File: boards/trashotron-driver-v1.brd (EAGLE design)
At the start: 76.2 x 63.5 mm, 11 parts, among them IC1 2967-MP6500, IC2 2967-MP6500, IC3 2967-MP6500, J2 455-1750-1-ND, J4 455-1750-1-ND, J6 455-1750-1-ND

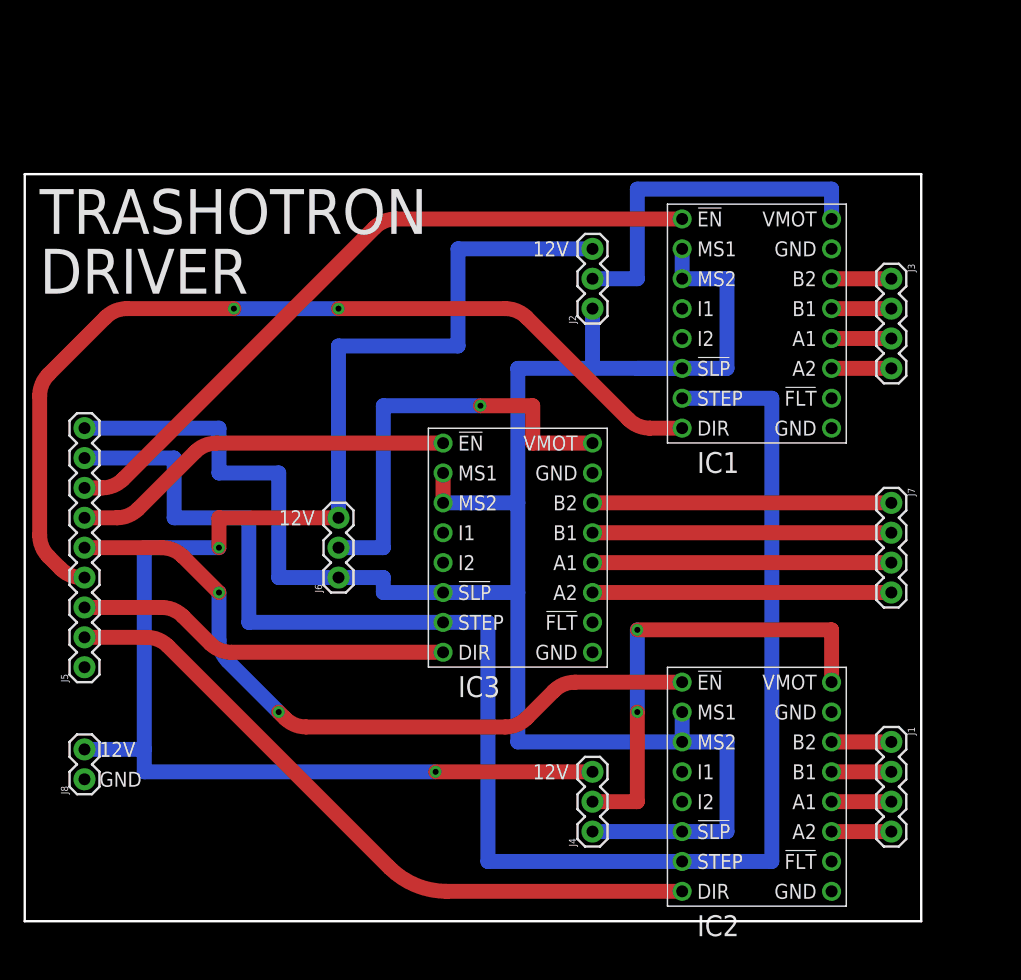
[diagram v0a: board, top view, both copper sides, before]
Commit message: board development and  a longer default glyph
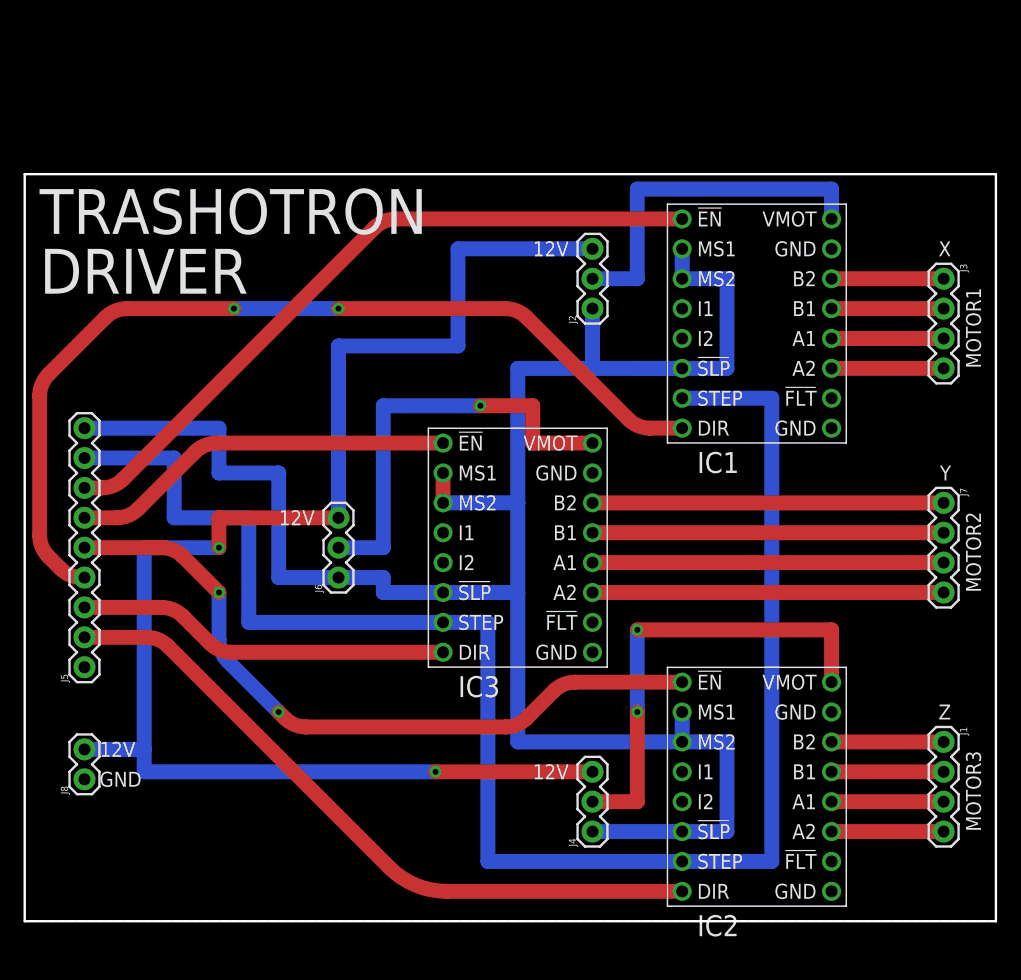
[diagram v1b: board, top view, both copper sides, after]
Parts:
- moved J1 4.45 mm to (78.1, 15.2)
- moved J3 4.45 mm to (78.1, 54.6)
- moved J7 4.45 mm to (78.1, 35.6)
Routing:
- net N$9: track 5.08 -> 9.53 mm
- net N$8: track 5.08 -> 9.53 mm
- net N$7: track 5.08 -> 9.53 mm
- net N$6: track 5.08 -> 9.53 mm
- net N$5: track 5.08 -> 9.53 mm
- net N$4: track 25.4 -> 29.8 mm
- net N$14: track 25.4 -> 29.8 mm
- net N$13: track 25.4 -> 29.8 mm
- net N$12: track 5.08 -> 9.53 mm
- net N$11: track 5.08 -> 9.53 mm
- net N$10: track 5.08 -> 9.53 mm
- net N$1: track 25.4 -> 29.8 mm
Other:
- board size 76.2 x 63.5 mm -> 82.5 x 63.5 mm
- board text added: "MOTOR1"
- board text added: "MOTOR2"
- board text added: "MOTOR3"
- board text added: "X"
- board text added: "Y"
- board text added: "Z"
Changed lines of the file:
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@@
 <board>
 <plain>
-<wire x1="76.2" y1="0" x2="76.2" y2="63.5" width="0.2032" layer="20"/>
-<wire x1="76.2" y1="63.5" x2="0" y2="63.5" width="0.2032" layer="20"/>
+<wire x1="82.55" y1="0" x2="82.55" y2="63.5" width="0.2032" layer="20"/>
+<wire x1="82.55" y1="63.5" x2="0" y2="63.5" width="0.2032" layer="20"/>
 <wire x1="0" y1="63.5" x2="0" y2="0" width="0.2032" layer="20"/>
-<wire x1="0" y1="0" x2="76.2" y2="0" width="0.2032" layer="20"/>
+<wire x1="0" y1="0" x2="82.55" y2="0" width="0.2032" layer="20"/>
 <wire x1="15.494" y1="0.508" x2="15.494" y2="29.21" width="0.0762" layer="51"/>
 <text x="-7.62" y="-5.08" size="2.286" layer="27">Arduino Wee v1.3</text>
@@
 <text x="43.18" y="12.065" size="1.27" layer="21">12V</text>
 <text x="21.59" y="33.655" size="1.27" layer="21">12V</text>
+<text x="81.28" y="7.62" size="1.27" layer="21" rot="R90">MOTOR3</text>
+<text x="81.28" y="27.94" size="1.27" layer="21" rot="R90">MOTOR2</text>
+<text x="81.28" y="46.99" size="1.27" layer="21" rot="R90">MOTOR1</text>
+<text x="78.74" y="18.415" size="1.27" layer="21" rot="R180">Z</text>
+<text x="78.74" y="38.735" size="1.27" layer="21" rot="R180">Y</text>
+<text x="78.74" y="57.785" size="1.27" layer="21" rot="R180">X</text>
 </plain>
 <attributes>
@@
 </autorouter>
 <elements>
-<element name="J3" library="SparkFun-Connectors" package="1X04" value="" x="73.66" y="54.61" smashed="yes" rot="R270">
-<attribute name="NAME" x="75.057" y="55.88" size="0.6096" layer="25" font="vector" ratio="20" rot="R270"/>
-<attribute name="PROD_ID" value="CONN-09696" x="73.66" y="54.61" size="1.778" layer="27" rot="R270" display="off"/>
-<attribute name="VALUE" x="71.628" y="55.88" size="0.6096" layer="27" font="vector" ratio="20" rot="R270"/>
-</element>
-<element name="J1" library="SparkFun-Connectors" package="1X04" value="" x="73.66" y="15.24" smashed="yes" rot="R270">
-<attribute name="NAME" x="75.057" y="16.51" size="0.6096" layer="25" font="vector" ratio="20" rot="R270"/>
-<attribute name="PROD_ID" value="CONN-09696" x="63.5" y="15.24" size="1.778" layer="27" rot="R270" display="off"/>
-<attribute name="VALUE" x="71.628" y="16.51" size="0.6096" layer="27" font="vector" ratio="20" rot="R270"/>
-</element>
-<element name="J7" library="SparkFun-Connectors" package="1X04" value="" x="73.66" y="35.56" smashed="yes" rot="R270">
-<attribute name="NAME" x="75.057" y="36.83" size="0.6096" layer="25" font="vector" ratio="20" rot="R270"/>
-<attribute name="PROD_ID" value="CONN-09696" x="64.135" y="35.56" size="1.778" layer="27" rot="R270" display="off"/>
-<attribute name="VALUE" x="71.628" y="36.83" size="0.6096" layer="27" font="vector" ratio="20" rot="R270"/>
+<element name="J3" library="SparkFun-Connectors" package="1X04" value="" x="78.105" y="54.61" smashed="yes" rot="R270">
+<attribute name="NAME" x="79.502" y="55.88" size="0.6096" layer="25" font="vector" ratio="20" rot="R270"/>
+<attribute name="PROD_ID" value="CONN-09696" x="78.105" y="54.61" size="1.778" layer="27" rot="R270" display="off"/>
+<attribute name="VALUE" x="76.073" y="55.88" size="0.6096" layer="27" font="vector" ratio="20" rot="R270"/>
+</element>
+<element name="J1" library="SparkFun-Connectors" package="1X04" value="" x="78.105" y="15.24" smashed="yes" rot="R270">
+<attribute name="NAME" x="79.502" y="16.51" size="0.6096" layer="25" font="vector" ratio="20" rot="R270"/>
+<attribute name="PROD_ID" value="CONN-09696" x="67.945" y="15.24" size="1.778" layer="27" rot="R270" display="off"/>
+<attribute name="VALUE" x="76.073" y="16.51" size="0.6096" layer="27" font="vector" ratio="20" rot="R270"/>
+</element>
+<element name="J7" library="SparkFun-Connectors" package="1X04" value="" x="78.105" y="35.56" smashed="yes" rot="R270">
+<attribute name="NAME" x="79.502" y="36.83" size="0.6096" layer="25" font="vector" ratio="20" rot="R270"/>
+<attribute name="PROD_ID" value="CONN-09696" x="68.58" y="35.56" size="1.778" layer="27" rot="R270" display="off"/>
+<attribute name="VALUE" x="76.073" y="36.83" size="0.6096" layer="27" font="vector" ratio="20" rot="R270"/>
 </element>
 <element name="IC1" library="pololu-stepper-driver" package="MP6500" value="2967-MP6500" x="62.23" y="50.8" smashed="yes">
@@
 <signal name="GND" class="1">
 <polygon width="0.254" layer="1" isolate="0.3048">
-<vertex x="76.2" y="0"/>
+<vertex x="82.55" y="0"/>
 <vertex x="0" y="0"/>
 <vertex x="0" y="63.5"/>
-<vertex x="76.2" y="63.5"/>
+<vertex x="82.55" y="63.5"/>
 </polygon>
 <polygon width="0.254" layer="16" isolate="0.3048">
-<vertex x="76.2" y="0"/>
+<vertex x="82.55" y="0"/>
 <vertex x="0" y="0"/>
 <vertex x="0" y="63.5"/>
-<vertex x="76.2" y="63.5"/>
+<vertex x="82.55" y="63.5"/>
 </polygon>
 <contactref element="IC1" pad="9"/>
@@
 <contactref element="J3" pad="1"/>
 <contactref element="IC1" pad="14"/>
-<wire x1="73.66" y1="54.61" x2="68.58" y2="54.61" width="1.27" layer="1"/>
+<wire x1="78.105" y1="54.61" x2="68.58" y2="54.61" width="1.27" layer="1"/>
 </signal>
 <signal name="N$6">
 <contactref element="J3" pad="2"/>
 <contactref element="IC1" pad="13"/>
-<wire x1="68.58" y1="52.07" x2="73.66" y2="52.07" width="1.27" layer="1"/>
+<wire x1="68.58" y1="52.07" x2="78.105" y2="52.07" width="1.27" layer="1"/>
 </signal>
 <signal name="N$7">
 <contactref element="J3" pad="3"/>
 <contactref element="IC1" pad="12"/>
-<wire x1="73.66" y1="49.53" x2="68.58" y2="49.53" width="1.27" layer="1"/>
+<wire x1="78.105" y1="49.53" x2="68.58" y2="49.53" width="1.27" layer="1"/>
 </signal>
 <signal name="N$8">
 <contactref element="J3" pad="4"/>
 <contactref element="IC1" pad="11"/>
-<wire x1="68.58" y1="46.99" x2="73.66" y2="46.99" width="1.27" layer="1"/>
+<wire x1="68.58" y1="46.99" x2="78.105" y2="46.99" width="1.27" layer="1"/>
 </signal>
 <signal name="N$9">
 <contactref element="J1" pad="1"/>
 <contactref element="IC2" pad="14"/>
-<wire x1="73.66" y1="15.24" x2="68.58" y2="15.24" width="1.27" layer="1"/>
+<wire x1="78.105" y1="15.24" x2="68.58" y2="15.24" width="1.27" layer="1"/>
 </signal>
 <signal name="N$10">
 <contactref element="J1" pad="2"/>
 <contactref element="IC2" pad="13"/>
-<wire x1="73.66" y1="12.7" x2="68.58" y2="12.7" width="1.27" layer="1"/>
+<wire x1="78.105" y1="12.7" x2="68.58" y2="12.7" width="1.27" layer="1"/>
 </signal>
 <signal name="N$11">
 <contactref element="J1" pad="3"/>
 <contactref element="IC2" pad="12"/>
-<wire x1="68.58" y1="10.16" x2="73.66" y2="10.16" width="1.27" layer="1"/>
+<wire x1="68.58" y1="10.16" x2="78.105" y2="10.16" width="1.27" layer="1"/>
 </signal>
 <signal name="N$12">
 <contactref element="J1" pad="4"/>
 <contactref element="IC2" pad="11"/>
-<wire x1="68.58" y1="7.62" x2="73.66" y2="7.62" width="1.27" layer="1"/>
+<wire x1="68.58" y1="7.62" x2="78.105" y2="7.62" width="1.27" layer="1"/>
 </signal>
 <signal name="DIR2">
@@
 <contactref element="IC3" pad="14"/>
 <contactref element="J7" pad="1"/>
-<wire x1="48.26" y1="35.56" x2="73.66" y2="35.56" width="1.27" layer="1"/>
+<wire x1="48.26" y1="35.56" x2="78.105" y2="35.56" width="1.27" layer="1"/>
 </signal>
 <signal name="N$4">
 <contactref element="IC3" pad="13"/>
 <contactref element="J7" pad="2"/>
-<wire x1="73.66" y1="33.02" x2="48.26" y2="33.02" width="1.27" layer="1"/>
+<wire x1="78.105" y1="33.02" x2="48.26" y2="33.02" width="1.27" layer="1"/>
 </signal>
 <signal name="N$13">
 <contactref element="IC3" pad="12"/>
 <contactref element="J7" pad="3"/>
-<wire x1="48.26" y1="30.48" x2="73.66" y2="30.48" width="1.27" layer="1"/>
+<wire x1="48.26" y1="30.48" x2="78.105" y2="30.48" width="1.27" layer="1"/>
 </signal>
 <signal name="N$14">
 <contactref element="IC3" pad="11"/>
 <contactref element="J7" pad="4"/>
-<wire x1="48.26" y1="27.94" x2="73.66" y2="27.94" width="1.27" layer="1"/>
+<wire x1="48.26" y1="27.94" x2="78.105" y2="27.94" width="1.27" layer="1"/>
 </signal>
 <signal name="5V">

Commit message: lots of work on pcb layout
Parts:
- removed J5: (no value), SparkFun-Connectors:1X09
- added C1: (no value), rcl:C050-050X075
- added J10: (no value), SparkFun-Connectors:1X02
- added J9: 455-1750-1-ND, SparkFun-Connectors:1X03
- added R3, R4, R5: (no value), SparkFun-Resistors:AXIAL-0.3
- added U2: LM358, SparkFun-IC-Amplifiers:DIP08
- J2: value 455-1750-1-ND -> (none); device SparkFun-Connectors:1X03 -> SparkFun-Connectors:1X08
- moved J4 68.1 mm to (64.8, 73.7), turned to 0 degrees
- moved J8 63.1 mm to (67.3, 1.91), turned to 0 degrees
- moved J2 46.0 mm to (2.54, 47.0), turned to 270 degrees
- moved J6 39.3 mm to (64.8, 19.7), turned to 0 degrees
- moved IC1 16.2 mm to (54.0, 64.8)
- moved J3 14.5 mm to (74.3, 68.6)
- moved IC3 13.6 mm to (54.0, 38.1)
- moved IC2 8.28 mm to (54.0, 10.8)
- moved J7 7.41 mm to (74.3, 41.9)
- moved J1 3.86 mm to (74.3, 14.6)
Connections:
- new net N$18: C1.2, R3.P$1, U2.6
- new net N$19: R4.P$1, R5.P$2, U2.5
- net 5V: now also J10.2, J4.2, J6.2, J9.2, U2.8; no longer J4.1, J5.9, J6.1
- net CLOCK: now also R3.P$2, R4.P$2, U2.7; no longer J5.8
- net DIR1: now also J2.5; no longer J5.4
- net DIR2: now also J2.6; no longer J5.3
- net DIR3: now also J2.7; no longer J5.2
- net EN1: now also J2.2; no longer J5.7
- net EN2: now also J2.3; no longer J5.6
- net EN3: now also J2.4; no longer J5.5
- net EXTPOW: now also J9.3; no longer J2.3
- net GND: now also C1.1, J10.1, J2.8, R5.P$1, U2.4; no longer J5.1
- net VMOT1: now also J4.1; no longer J2.2
- net VMOT2: now also J9.1; no longer J6.2
- net VMOT3: now also J6.1; no longer J4.2
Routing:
- net 5V: track 171.4 -> 263.5 mm, vias 0 -> 2
- net EXTPOW: track 125.7 -> 71.8 mm, vias 2 -> 0
- net VMOT3: track 39.4 -> 4.44 mm, vias 2 -> 0
- net VMOT2: track 36.8 -> 4.44 mm, vias 1 -> 0
- net N$18: track 0.00 -> 31.1 mm
- net DIR1: track 79.3 -> 51.8 mm
- net VMOT1: track 30.5 -> 4.44 mm
- net N$19: track 0.00 -> 20.3 mm
- net N$4: track 29.8 -> 14.0 mm
- net N$14: track 29.8 -> 14.0 mm
- net N$13: track 29.8 -> 14.0 mm
- net N$1: track 29.8 -> 14.0 mm
- net DIR2: track 31.7 -> 46.2 mm, vias 0 -> 2
- net EN2: track 32.8 -> 46.1 mm
- net EN3: track 60.9 -> 51.8 mm, vias 2 -> 0
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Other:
- board size 82.5 x 63.5 mm -> 76.2 x 76.2 mm
- board text added: "0.1uF"
- board text added: "4.7k"
- board text added: "5V"
- board text added: "DIR1"
- board text added: "DIR2"
- board text added: "DIR3"
- board text added: "EN1"
- board text added: "EN2"
- board text added: "EN3"
- board text added: "LM358p"
- board text added: "TRASHOTRON DRIVER"
- board text removed: "DRIVER"
- board text removed: "TRASHOTRON"
